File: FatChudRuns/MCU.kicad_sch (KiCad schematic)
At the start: 28 parts, among them J2 Z-21320110021001, J3 FTSH-107-01-L-DV-K-P, SW1 TS-1187A-B-A-B, SW5 1825360-3, U1 STM32F107RBT6, Y2 ABM8G-25.000MHZ-B4Y-T

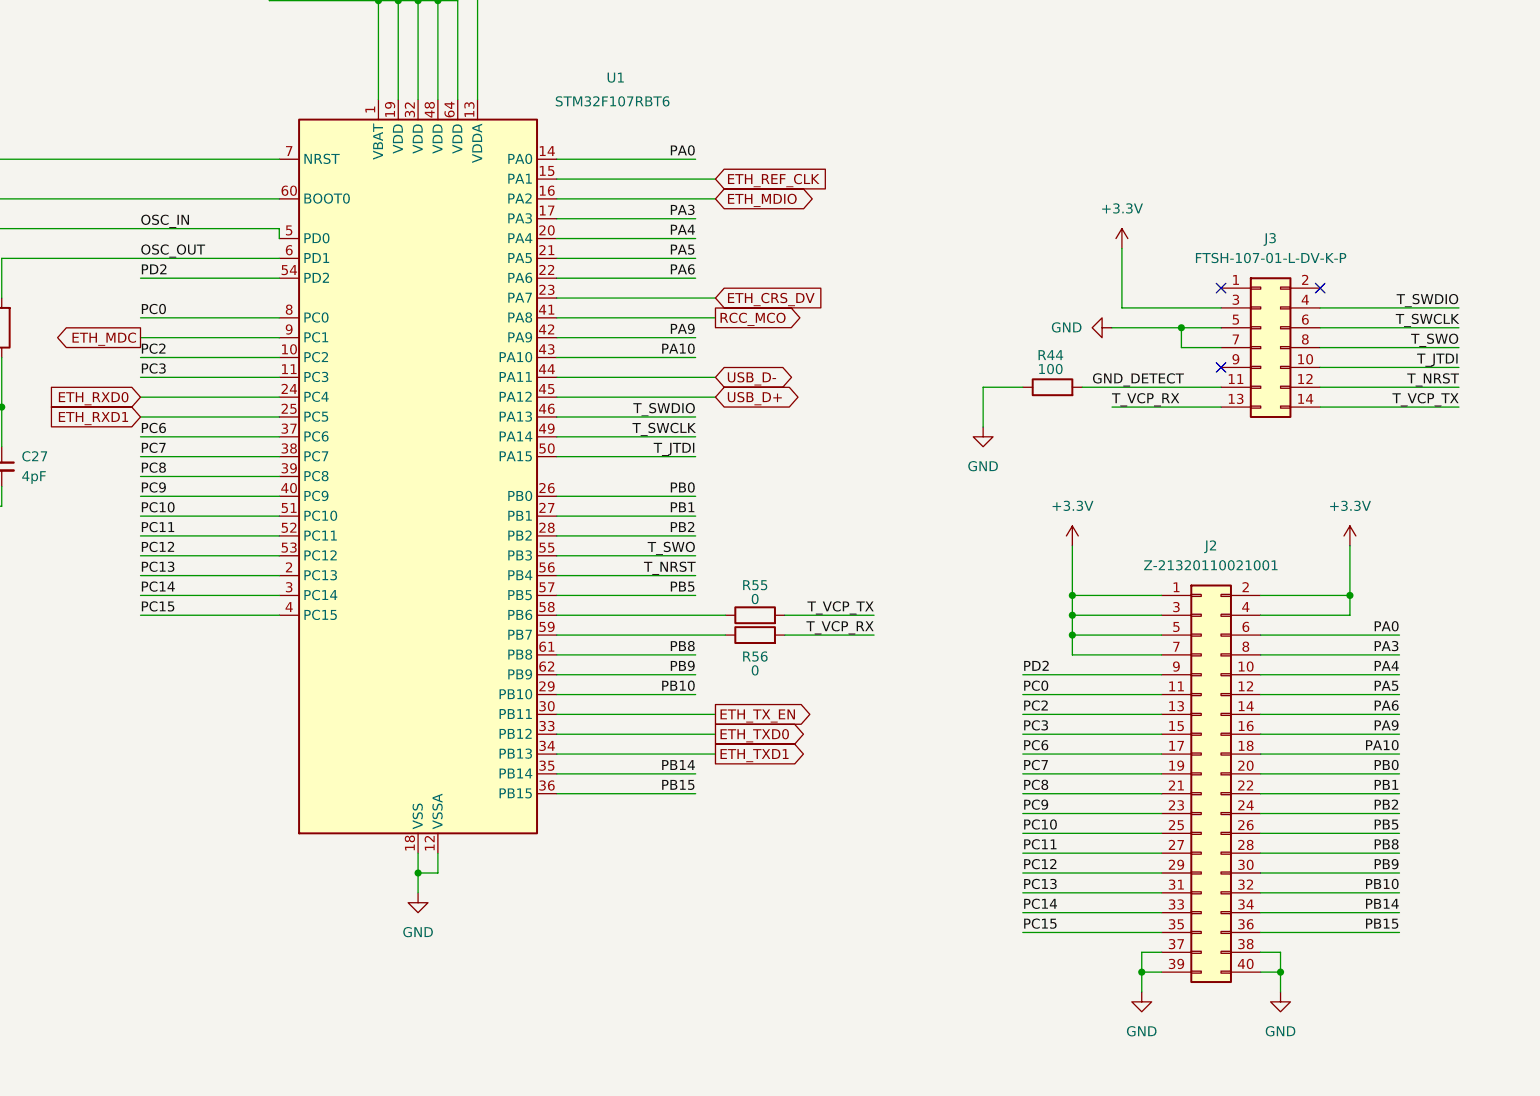
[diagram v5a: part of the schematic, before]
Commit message: finished initial layout, removed some gpio pins and reorganized them
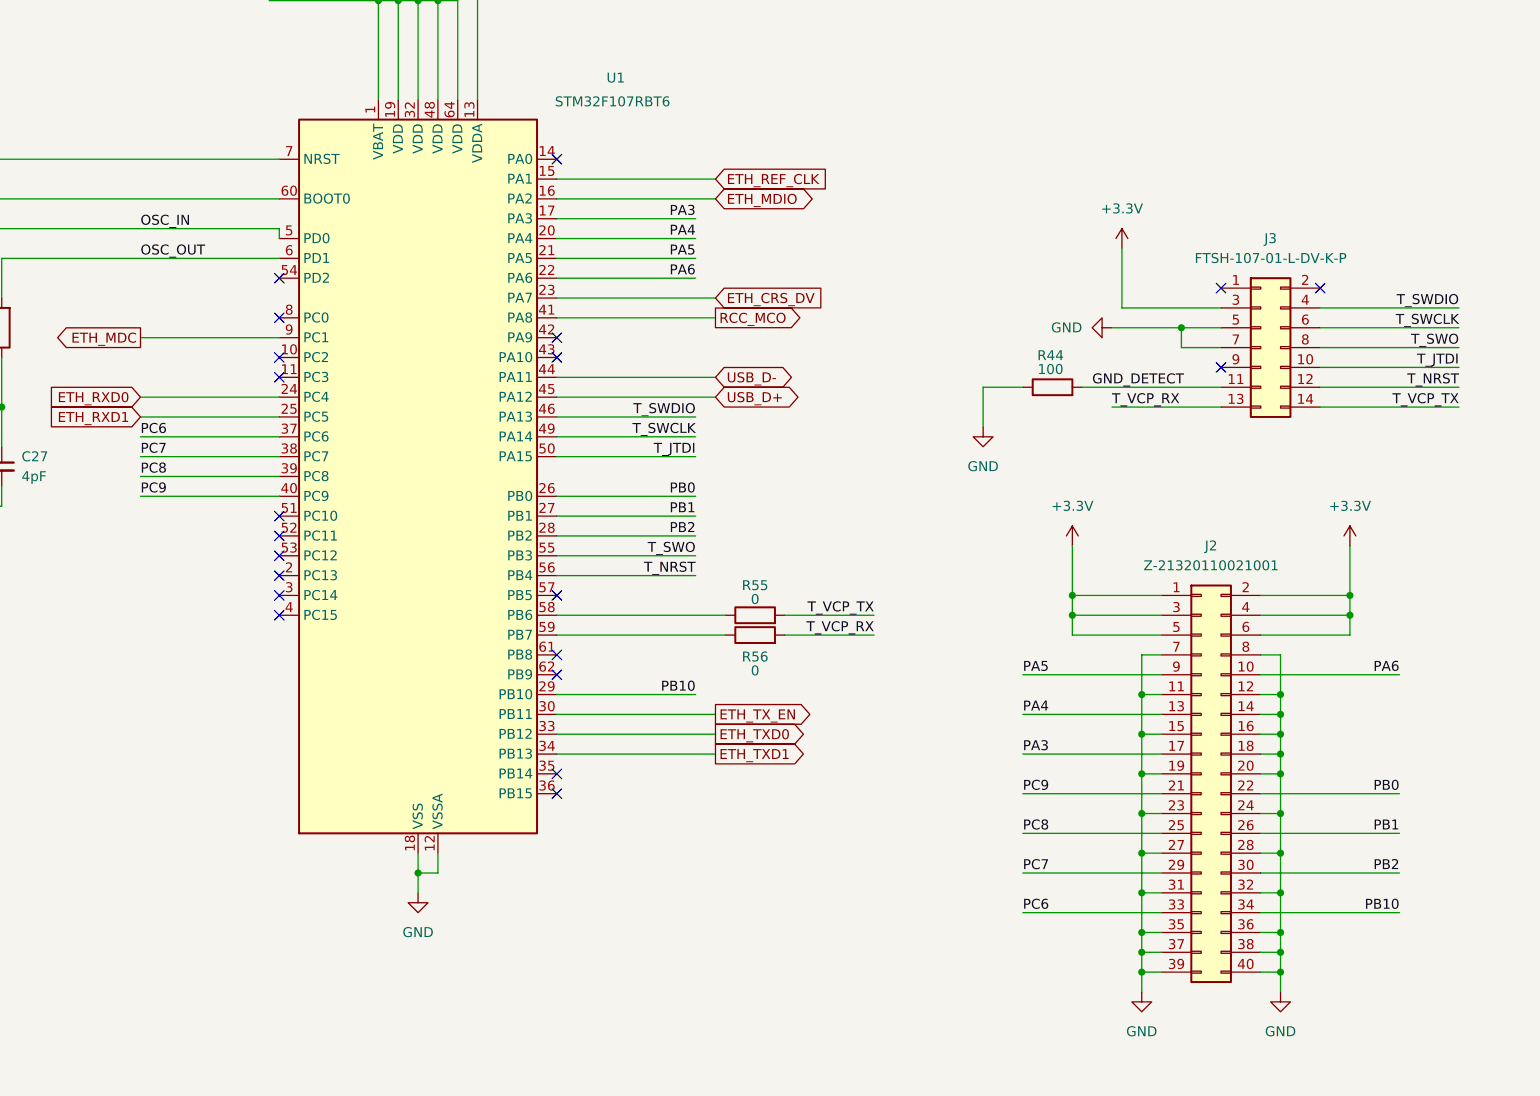
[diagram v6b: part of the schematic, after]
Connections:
- net +3.3V: now also J2.6 (Pin_6); no longer J2.7 (Pin_7)
- net GND: now also J2.11 (Pin_11), J2.12 (Pin_12), J2.14 (Pin_14), J2.15 (Pin_15), J2.16 (Pin_16), J2.18 (Pin_18), J2.19 (Pin_19), J2.20 (Pin_20), J2.23 (Pin_23), J2.24 (Pin_24), J2.27 (Pin_27), J2.28 (Pin_28), J2.31 (Pin_31), J2.32 (Pin_32), J2.35 (Pin_35), J2.36 (Pin_36), J2.7 (Pin_7), J2.8 (Pin_8)
- net PA3: now also J2.17 (Pin_17); no longer J2.8 (Pin_8)
- net PA4: now also J2.13 (Pin_13); no longer J2.10 (Pin_10)
- net PA5: now also J2.9 (Pin_9); no longer J2.12 (Pin_12)
- net PA6: now also J2.10 (Pin_10); no longer J2.14 (Pin_14)
- net PB0: now also J2.22 (Pin_22); no longer J2.20 (Pin_20)
- net PB1: now also J2.26 (Pin_26); no longer J2.22 (Pin_22)
- net PB10: now also J2.34 (Pin_34); no longer J2.32 (Pin_32)
- net PB2: now also J2.30 (Pin_30); no longer J2.24 (Pin_24)
- net PC6: now also J2.33 (Pin_33); no longer J2.17 (Pin_17)
- net PC7: now also J2.29 (Pin_29); no longer J2.19 (Pin_19)
- net PC8: now also J2.25 (Pin_25); no longer J2.21 (Pin_21)
- net PC9: now also J2.21 (Pin_21); no longer J2.23 (Pin_23)
- net PA0: no longer names the net of U1.14 (PA0)
- net PA0: no longer J2.6 (Pin_6)
- net PA10: no longer names the net of U1.43 (PA10)
- net PA10: no longer J2.18 (Pin_18)
- net PA9: no longer names the net of U1.42 (PA9)
- net PA9: no longer J2.16 (Pin_16)
- net PB14: no longer names the net of U1.35 (PB14)
- net PB14: no longer J2.34 (Pin_34)
- net PB15: no longer names the net of U1.36 (PB15)
- net PB15: no longer J2.36 (Pin_36)
- net PB5: no longer names the net of U1.57 (PB5)
- net PB5: no longer J2.26 (Pin_26)
- net PB8: no longer names the net of U1.61 (PB8)
- net PB8: no longer J2.28 (Pin_28)
- net PB9: no longer names the net of U1.62 (PB9)
- net PB9: no longer J2.30 (Pin_30)
- net PC0: no longer names the net of U1.8 (PC0)
- net PC0: no longer J2.11 (Pin_11)
- net PC10: no longer names the net of U1.51 (PC10)
- net PC10: no longer J2.25 (Pin_25)
- net PC11: no longer names the net of U1.52 (PC11)
- net PC11: no longer J2.27 (Pin_27)
- net PC12: no longer names the net of U1.53 (PC12)
- net PC12: no longer J2.29 (Pin_29)
- net PC13: no longer names the net of U1.2 (PC13)
- net PC13: no longer J2.31 (Pin_31)
- net PC14: no longer names the net of U1.3 (PC14)
- net PC14: no longer J2.33 (Pin_33)
- net PC15: no longer names the net of U1.4 (PC15)
- net PC15: no longer J2.35 (Pin_35)
- net PC2: no longer names the net of U1.10 (PC2)
- net PC2: no longer J2.13 (Pin_13)
- net PC3: no longer names the net of U1.11 (PC3)
- net PC3: no longer J2.15 (Pin_15)
- net PD2: no longer names the net of U1.54 (PD2)
- net PD2: no longer J2.9 (Pin_9)
- no-connect marks 5 -> 23

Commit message: updated 10uF to 0805, completed BOM, sent to fab
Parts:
- C1: footprint Capacitor_SMD:C_0603_1608Metric -> Capacitor_SMD:C_0805_2012Metric; JLCPCB Part # (none) -> C2167271; Manufacturer Number (none) -> C0805C106K4PAC
- C2, C25, C3, C4, C5, C6, C8: JLCPCB Part # (none) -> C2181816; Manufacturer Number (none) -> C0603C104K4RAC
- C26, C27: JLCPCB Part # (none) -> C309461; Manufacturer Number (none) -> CC0603BRNPO9BN4R0
- C7: JLCPCB Part # (none) -> C561804; Manufacturer Number (none) -> C0603C105K4PACAUTO
- D3, D4: JLCPCB Part # (none) -> C2935146; Manufacturer Number (none) -> ESDA6V1SC5
- J2: JLCPCB Part # (none) -> C193453; Manufacturer Number (none) -> Z-21320110021001
- J3: JLCPCB Part # (none) -> C5345538; Manufacturer Number (none) -> FTSH-107-01-L-DV-K-P
- R1, R2: JLCPCB Part # (none) -> C99782; Manufacturer Number (none) -> RC0603FR-074K7L
- R44: JLCPCB Part # (none) -> C105588; Manufacturer Number (none) -> RC0603FR-07100RL
- R52: JLCPCB Part # (none) -> C107696; Manufacturer Number (none) -> RC0603FR-07220RL
- R55, R56, R57: JLCPCB Part # (none) -> C95177; Manufacturer Number (none) -> RC0603JR-070RL
- SW1: JLCPCB Part # (none) -> C318884; Manufacturer Number (none) -> TS-1187A-B-A-B
- SW5: JLCPCB Part # (none) -> C574798; Manufacturer Number (none) -> 1825360-3
- U1: JLCPCB Part # (none) -> C16918; Manufacturer Number (none) -> STM32F107RBT6
- Y2: JLCPCB Part # (none) -> C596913; Manufacturer Number (none) -> ABM8G-25.000MHZ-B4Y-T
